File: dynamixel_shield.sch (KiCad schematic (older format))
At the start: 27 parts, among them P1 BARREL_JACK, P2 CONN_01X02, P3 CONN_01X03, P4 CONN_01X03, P5 CONN_01X03, P6 CONN_01X03, P7 CONN_01X03, P8 CONN_01X03, P9 CONN_01X03, Q1 MOSFET_N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

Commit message: update pcb with new resistors
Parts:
- R7: footprint (none) -> Resistors_SMD:R_0603_HandSoldering
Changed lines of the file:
@@
 F 0 "R7" V 6330 2550 50  0000 C CNN
 F 1 "10K" V 6250 2550 50  0000 C CNN
-F 2 "" V 6180 2550 50  0000 C CNN
+F 2 "Resistors_SMD:R_0603_HandSoldering" V 6180 2550 50  0001 C CNN
 F 3 "" H 6250 2550 50  0000 C CNN
 	1    6250 2550

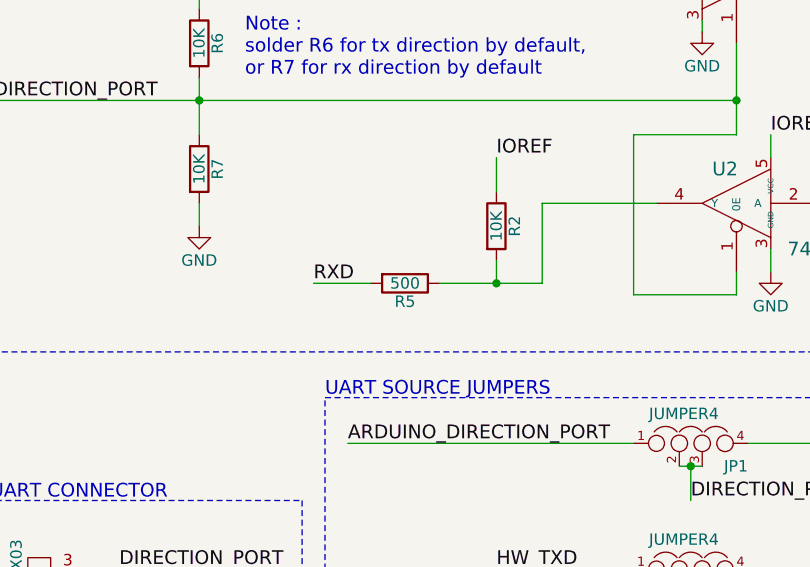
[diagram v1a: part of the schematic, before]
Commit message: update resistor value
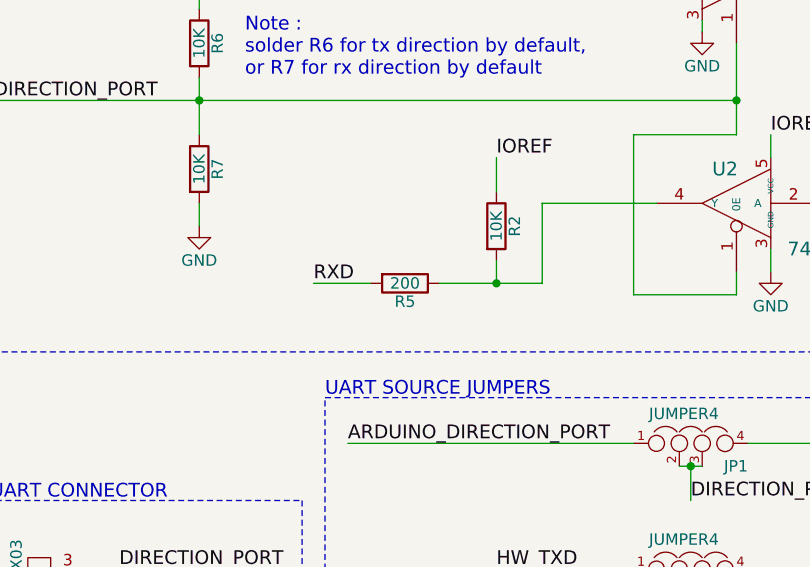
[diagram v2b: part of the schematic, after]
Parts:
- R5: value 500 -> 200
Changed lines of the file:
@@
 P 7150 3050
 F 0 "R5" V 7230 3050 50  0000 C CNN
-F 1 "500" V 7150 3050 50  0000 C CNN
+F 1 "200" V 7150 3050 50  0000 C CNN
 F 2 "Resistors_SMD:R_0603_HandSoldering" V 7080 3050 50  0001 C CNN
 F 3 "" H 7150 3050 50  0000 C CNN

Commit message: tweak some components placement
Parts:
- D1: symbol LED -> LED-RESCUE-dynamixel_shield
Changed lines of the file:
@@
 EESchema Schematic File Version 2
+LIBS:dynamixel_shield-rescue
 LIBS:power
 LIBS:device
@@
 $EndComp
 $Comp
-L LED D1
+L LED-RESCUE-dynamixel_shield D1
 U 1 1 57BDD735
 P 1200 3700

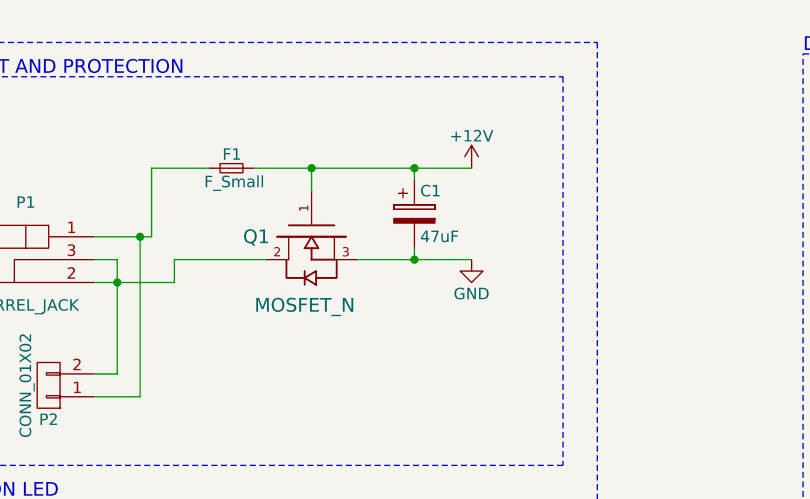
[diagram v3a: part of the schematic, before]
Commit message: increase capacitors, add a few vias
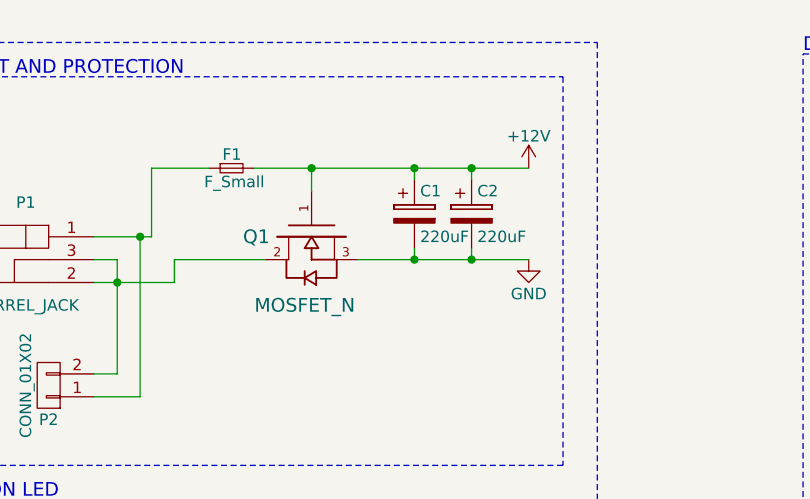
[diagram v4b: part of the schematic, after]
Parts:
- added C2: 220uF, Capacitors_SMD:CP_Elec_6.3x7.7, symbol CP
- C1: value 47uF -> 220uF; footprint Capacitors_SMD:c_elec_6.3x5.8 -> Capacitors_SMD:CP_Elec_6.3x7.7
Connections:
- net +12V: now also C2.1
- net GND: now also C2.2
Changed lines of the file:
@@
 L GND #PWR04
 U 1 1 57B2328F
-P 3300 1650
-F 0 "#PWR04" H 3300 1400 50  0001 C CNN
-F 1 "GND" H 3300 1500 50  0000 C CNN
-F 2 "" H 3300 1650 50  0000 C CNN
-F 3 "" H 3300 1650 50  0000 C CNN
-	1    3300 1650
+P 3550 1650
+F 0 "#PWR04" H 3550 1400 50  0001 C CNN
+F 1 "GND" H 3550 1500 50  0000 C CNN
+F 2 "" H 3550 1650 50  0000 C CNN
+F 3 "" H 3550 1650 50  0000 C CNN
+	1    3550 1650
 	1    0    0    -1
 $EndComp
@@
 L +12V #PWR018
 U 1 1 57B5F255
-P 3300 1250
-F 0 "#PWR018" H 3300 1100 50  0001 C CNN
-F 1 "+12V" H 3300 1390 50  0000 C CNN
-F 2 "" H 3300 1250 50  0000 C CNN
-F 3 "" H 3300 1250 50  0000 C CNN
-	1    3300 1250
+P 3550 1250
+F 0 "#PWR018" H 3550 1100 50  0001 C CNN
+F 1 "+12V" H 3550 1390 50  0000 C CNN
+F 2 "" H 3550 1250 50  0000 C CNN
+F 3 "" H 3550 1250 50  0000 C CNN
+	1    3550 1250
 	1    0    0    -1
 $EndComp
@@
 P 3050 1450
 F 0 "C1" H 3075 1550 50  0000 L CNN
-F 1 "47uF" H 3075 1350 50  0000 L CNN
-F 2 "Capacitors_SMD:c_elec_6.3x5.8" H 3088 1300 50  0001 C CNN
+F 1 "220uF" H 3075 1350 50  0000 L CNN
+F 2 "Capacitors_SMD:CP_Elec_6.3x7.7" H 3088 1300 50  0001 C CNN
 F 3 "" H 3050 1450 50  0000 C CNN
 	1    3050 1450
@@
 	2000 1650 2400 1650
 Wire Wire Line
-	2350 1250 3300 1250
+	2350 1250 3550 1250
 Wire Wire Line
 	1750 1650 1750 2150
@@
 	600  4450 600  700
 Wire Wire Line
-	3300 1650 2800 1650
+	2800 1650 3550 1650
 Wire Wire Line
 	2150 1250 1900 1250
@@
 $EndComp
 $Comp
-L GND #PWR?
+L GND #PWR025
 U 1 1 5802386A
 P 6250 2800
-F 0 "#PWR?" H 6250 2550 50  0001 C CNN
+F 0 "#PWR025" H 6250 2550 50  0001 C CNN
 F 1 "GND" H 6250 2650 50  0000 C CNN
 F 2 "" H 6250 2800 50  0000 C CNN
@@
 Text Notes 6450 2150 0    60   ~ 0
 Note : \nsolder R6 for tx direction by default, \nor R7 for rx direction by default
+$Comp
+L CP C2
+U 1 1 5C91DFFD
+P 3300 1450
+F 0 "C2" H 3325 1550 50  0000 L CNN
+F 1 "220uF" H 3325 1350 50  0000 L CNN
+F 2 "Capacitors_SMD:CP_Elec_6.3x7.7" H 3338 1300 50  0001 C CNN
+F 3 "" H 3300 1450 50  0000 C CNN
+	1    3300 1450
+	1    0    0    -1
+$EndComp
+Wire Wire Line
+	3300 1300 3300 1250
+Connection ~ 3300 1250
+Wire Wire Line
+	3300 1600 3300 1650
+Connection ~ 3300 1650
 $EndSCHEMATC
